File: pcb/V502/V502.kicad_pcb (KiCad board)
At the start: 4 copper layers, 40 parts, among them J1 Conn_01x30_Pin, J2 Conn_01x30_Pin, J3 Conn_01x30_Pin, J4 Conn_01x30_Pin, U1 74LS670, U10 74LS670, U11 74LS283, U12 74LS157, U13 74LS574, U14 74LS574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

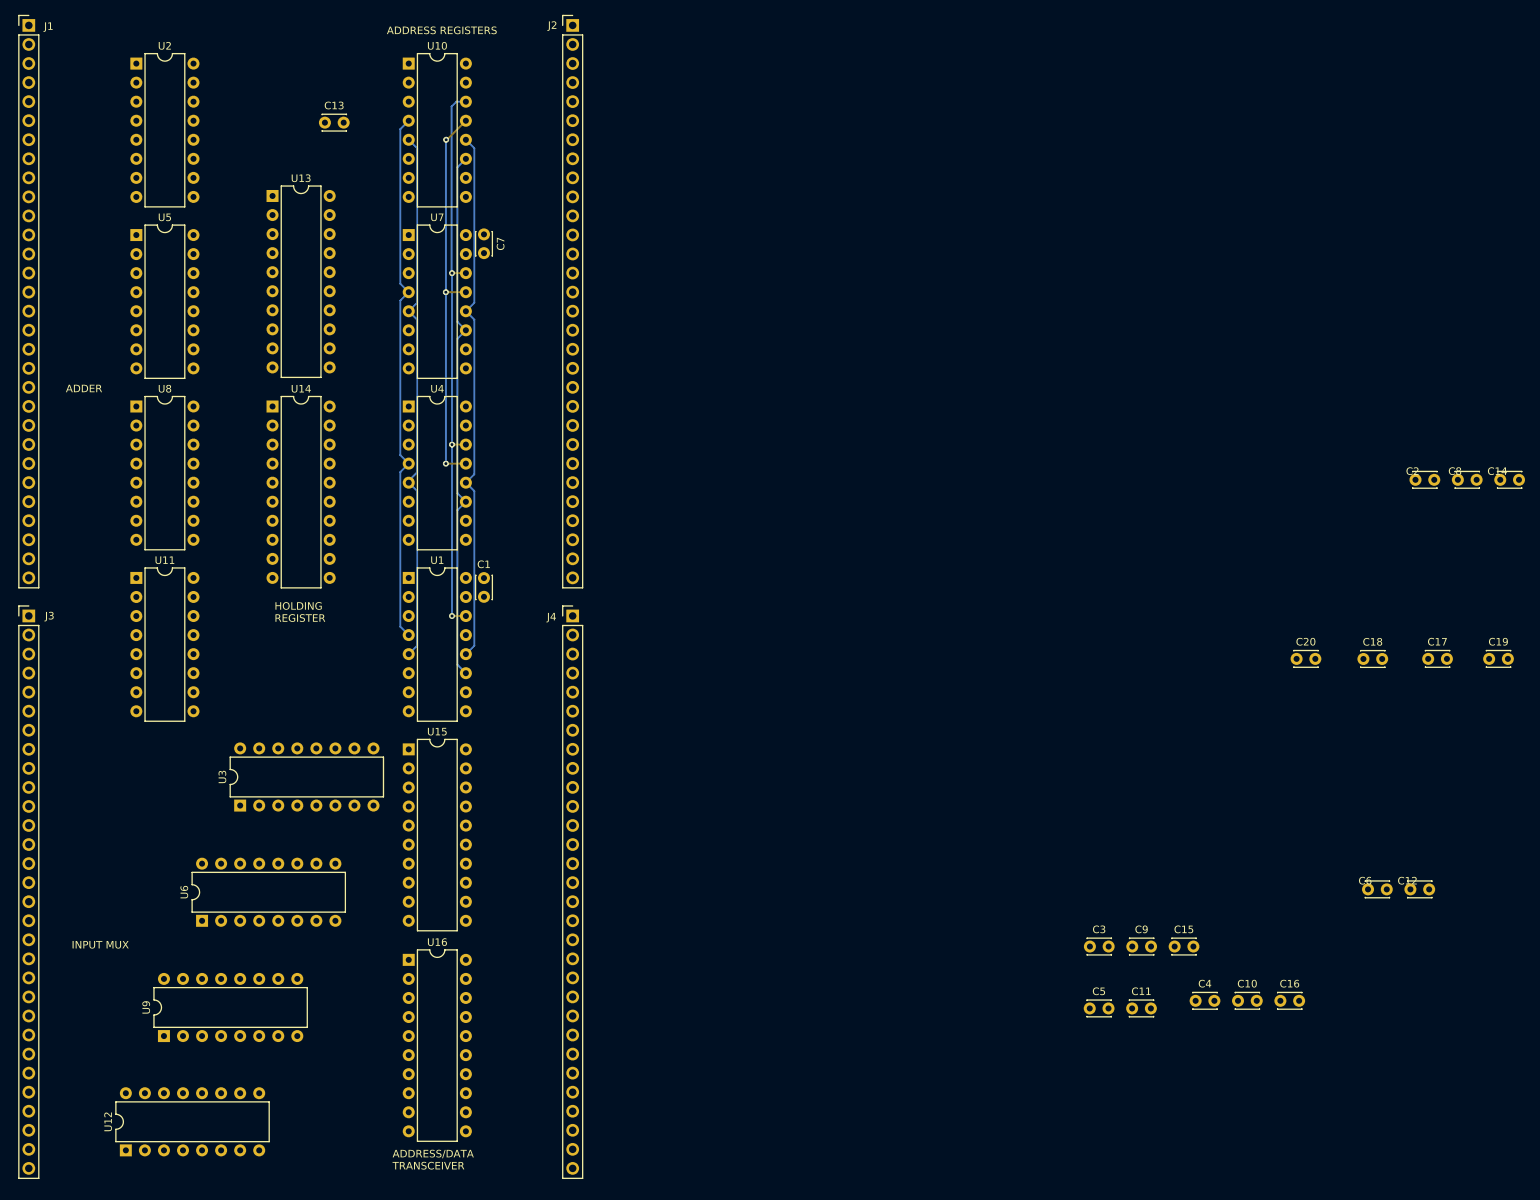
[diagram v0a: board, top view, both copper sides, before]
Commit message: V502 board almost completely routed.
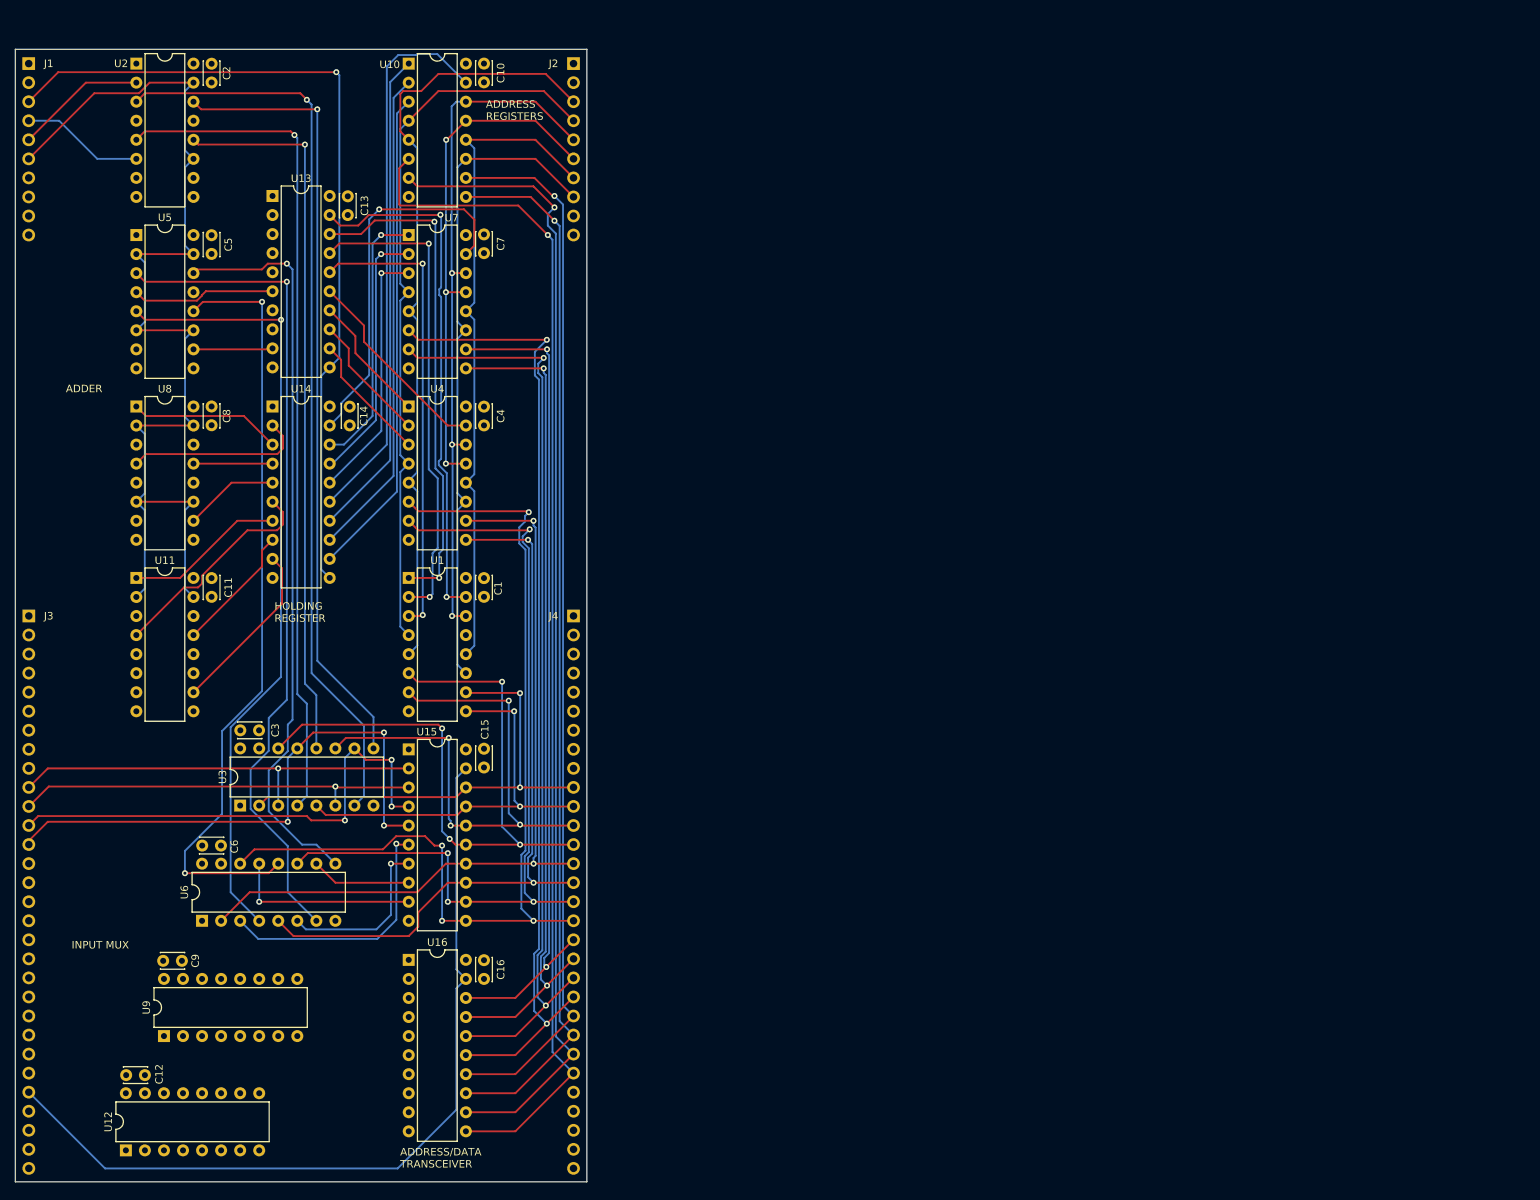
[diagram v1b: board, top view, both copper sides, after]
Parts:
- removed C17, C18, C19, C20: C_Small, Capacitor_THT:C_Disc_D3.0mm_W2.0mm_P2.50mm
- J1, J2: value Conn_01x30_Pin -> Conn_01x10_Pin; footprint Connector_PinHeader_2.54mm:PinHeader_1x30_P2.54mm_Vertical -> Connector_PinHeader_2.54mm:PinHeader_1x10_P2.54mm_Vertical; moved to B.Cu
- J3, J4: moved to B.Cu
- moved C12 173.0 mm to (49.4, 167.9)
- moved C2 169.8 mm to (60.8, 33.0), turned to -90 degrees
- moved C8 166.5 mm to (60.8, 78.7), turned to -90 degrees
- moved C10 160.4 mm to (97.2, 33.0), turned to -90 degrees
- moved C5 156.0 mm to (60.8, 55.9), turned to -90 degrees
- moved C6 155.6 mm to (59.6, 137.3)
- moved C14 153.7 mm to (79.2, 78.8), turned to -90 degrees
- moved C11 135.5 mm to (60.8, 101.6), turned to -90 degrees
- moved C9 129.2 mm to (54.4, 152.7)
- moved C4 123.6 mm to (97.2, 78.8), turned to -90 degrees
- moved C3 116.9 mm to (64.7, 121.9)
- moved C16 106.3 mm to (97.2, 152.6), turned to -90 degrees
- moved C15 95.8 mm to (97.2, 124.4), turned to -90 degrees
- moved C13 10.3 mm to (79.0, 50.7), turned to -90 degrees
- moved J2 5.09 mm to (109.1, 33.0), turned to 180 degrees
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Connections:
- J1 pad 10: unconnected-(J1-Pin_10-Pad10) -> VCC
- J1 pad 3: unconnected-(J1-Pin_3-Pad3) -> SYSCLK
- J1 pad 4: unconnected-(J1-Pin_4-Pad4) -> SRC2:0
- J1 pad 5: unconnected-(J1-Pin_5-Pad5) -> SRC2:1
- J1 pad 6: unconnected-(J1-Pin_6-Pad6) -> SRC2:2
- J1 pad 7: unconnected-(J1-Pin_7-Pad7) -> VCC
- J1 pad 8: unconnected-(J1-Pin_8-Pad8) -> VCC
- J1 pad 9: unconnected-(J1-Pin_9-Pad9) -> VCC
- J2 pad 10: unconnected-(J2-Pin_10-Pad10) -> VCC
- J2 pad 3: unconnected-(J2-Pin_3-Pad3) -> Ra
- J2 pad 4: unconnected-(J2-Pin_4-Pad4) -> Rb
- J2 pad 5: unconnected-(J2-Pin_5-Pad5) -> Wa
- J2 pad 6: unconnected-(J2-Pin_6-Pad6) -> Wb
- J2 pad 7: unconnected-(J2-Pin_7-Pad7) -> ~{Ew}
- J2 pad 8: unconnected-(J2-Pin_8-Pad8) -> ~{Er}
- J2 pad 9: unconnected-(J2-Pin_9-Pad9) -> VCC
- J3 pad 10: SYSDATA4 -> SYSDATA0
- J3 pad 11: SYSDATA5 -> SYSDATA1
- J3 pad 12: SYSDATA6 -> SYSDATA2
- J3 pad 13: SYSDATA7 -> SYSDATA3
- J3 pad 14: unconnected-(J3-Pin_14-Pad14) -> SYSDATA4
- J3 pad 15: unconnected-(J3-Pin_15-Pad15) -> SYSDATA5
- J3 pad 16: unconnected-(J3-Pin_16-Pad16) -> SYSDATA6
- J3 pad 17: unconnected-(J3-Pin_17-Pad17) -> SYSDATA7
- J3 pad 26: unconnected-(J3-Pin_26-Pad26) -> ~{AtoD}
- J3 pad 27: unconnected-(J3-Pin_27-Pad27) -> GND
- J3 pad 28: unconnected-(J3-Pin_28-Pad28) -> GND
- J3 pad 3: unconnected-(J3-Pin_3-Pad3) -> VCC
- J3 pad 4: unconnected-(J3-Pin_4-Pad4) -> VCC
- J3 pad 5: unconnected-(J3-Pin_5-Pad5) -> VCC
- J3 pad 6: SYSDATA0 -> VCC
- J3 pad 7: SYSDATA1 -> VCC
- J3 pad 8: SYSDATA2 -> VCC
- J3 pad 9: SYSDATA3 -> SELDATA
- J4 pad 26: unconnected-(J4-Pin_26-Pad26) -> GND
- J4 pad 27: unconnected-(J4-Pin_27-Pad27) -> GND
- J4 pad 28: unconnected-(J4-Pin_28-Pad28) -> GND
- J4 pad 3: unconnected-(J4-Pin_3-Pad3) -> VCC
- J4 pad 4: unconnected-(J4-Pin_4-Pad4) -> VCC
- J4 pad 5: unconnected-(J4-Pin_5-Pad5) -> VCC
- J4 pad 6: unconnected-(J4-Pin_6-Pad6) -> VCC
- J4 pad 7: unconnected-(J4-Pin_7-Pad7) -> VCC
- J4 pad 8: unconnected-(J4-Pin_8-Pad8) -> VCC
- J4 pad 9: unconnected-(J4-Pin_9-Pad9) -> VCC
- U11 pad 7: GND -> Net-(U11-C0)
- U13 pad 1: unconnected-(U13-OE-Pad1) -> GND
- U13 pad 11: unconnected-(U13-Cp-Pad11) -> SYSCLK
- U14 pad 1: unconnected-(U14-OE-Pad1) -> GND
- U14 pad 11: unconnected-(U14-Cp-Pad11) -> SYSCLK
- U15 pad 1: unconnected-(U15-A->B-Pad1) -> GND
- U15 pad 19: unconnected-(U15-CE-Pad19) -> ~{AtoD}
- U16 pad 1: unconnected-(U16-A->B-Pad1) -> GND
- U16 pad 19: unconnected-(U16-CE-Pad19) -> ~{AtoD}
- U2 pad 9: unconnected-(U2-C4-Pad9) -> Net-(U2-C4)
- U5 pad 7: GND -> Net-(U2-C4)
- U5 pad 9: unconnected-(U5-C4-Pad9) -> Net-(U5-C4)
- U8 pad 7: GND -> Net-(U5-C4)
- U8 pad 9: unconnected-(U8-C4-Pad9) -> Net-(U11-C0)
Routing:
- net SYSADDR15: track 0.00 -> 158.9 mm, vias 0 -> 1
- net SYSADDR14: track 0.00 -> 153.3 mm, vias 0 -> 1
- net SRC2:2: track 0.00 -> 144.5 mm
- net SYSADDR12: track 0.00 -> 140.8 mm, vias 0 -> 1
- net SYSADDR13: track 0.00 -> 140.3 mm, vias 0 -> 1
- net SYSADDR11: track 0.00 -> 129.5 mm, vias 0 -> 2
- net SYSADDR7: track 0.00 -> 129.3 mm, vias 0 -> 4
- net SYSADDR10: track 0.00 -> 123.6 mm, vias 0 -> 2
- net A1: track 0.00 -> 121.3 mm, vias 0 -> 1
- net A0: track 0.00 -> 112.4 mm, vias 0 -> 1
- net SYSCLK: track 0.00 -> 111.7 mm, vias 0 -> 1
- net SYSADDR6: track 0.00 -> 111.7 mm, vias 0 -> 4
- net ~{AtoD}: track 0.00 -> 111.6 mm
- net A5: track 0.00 -> 111.4 mm, vias 0 -> 1
- net SYSADDR8: track 0.00 -> 111.2 mm, vias 0 -> 2
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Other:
- board outline added: 76.2 x 151 mm

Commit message: V502 is complete. Freezing it permanently.
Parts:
- moved C1 2.50 mm to (97.2, 101.6), turned to -90 degrees
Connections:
- J2 pad 1: VCC -> GND
- J2 pad 10: VCC -> GND
- J2 pad 2: VCC -> GND
- J2 pad 9: VCC -> GND
- J3 pad 27: GND -> VCC
- J3 pad 28: GND -> VCC
- J3 pad 29: GND -> VCC
- J3 pad 30: GND -> VCC
- J4 pad 1: VCC -> GND
- J4 pad 2: VCC -> GND
- J4 pad 3: VCC -> GND
- J4 pad 4: VCC -> GND
- J4 pad 5: VCC -> GND
- J4 pad 6: VCC -> GND
- J4 pad 7: VCC -> GND
- J4 pad 8: VCC -> GND
- J4 pad 9: VCC -> GND
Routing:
- net SELDATA: track 0.00 -> 181.7 mm, vias 0 -> 7
- net A9: track 0.00 -> 91.8 mm, vias 0 -> 1
- net A10: track 0.00 -> 85.0 mm, vias 0 -> 1
- net A14: track 0.00 -> 83.3 mm, vias 0 -> 1
- net A13: track 0.00 -> 83.1 mm, vias 0 -> 1
- net A8: track 0.00 -> 82.3 mm, vias 0 -> 1
- net A12: track 0.00 -> 76.1 mm, vias 0 -> 1
- net A11: track 0.00 -> 75.5 mm, vias 0 -> 1
- net SYSDATA12: track 0.00 -> 74.9 mm, vias 0 -> 3
- net A15: track 0.00 -> 73.8 mm, vias 0 -> 1
- net SYSDATA8: track 0.00 -> 68.0 mm, vias 0 -> 3
- net SYSDATA13: track 0.00 -> 67.5 mm, vias 0 -> 3
- net SYSDATA10: track 0.00 -> 64.1 mm, vias 0 -> 2
- net SYSDATA9: track 0.00 -> 63.9 mm, vias 0 -> 2
- net SYSDATA11: track 0.00 -> 61.6 mm, vias 0 -> 2
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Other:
- board size 76.2 x 151 mm -> 76.2 x 151.8 mm
